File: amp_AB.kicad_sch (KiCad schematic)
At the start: 15 parts, among them J1 Power, J2 Audio, J3 Conn_01x02, Q1 TIP141, Q2 TIP146, U2 NE5532

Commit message: EL HUEVO SAPE
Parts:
- added C5, C6: 100n, Capacitor_SMD:CP_Elec_10x10, symbol ltspice:cap
- added C7, C8: 470µ, symbol ltspice:polcap
- C1: footprint (none) -> Capacitor_THT:CP_Radial_D13.0mm_P7.50mm
- C4: footprint (none) -> Capacitor_THT:CP_Radial_D10.0mm_P7.50mm
- R3: footprint (none) -> Resistor_SMD:R_01005_0402Metric
- R4: footprint (none) -> Resistor_THT:R_Axial_DIN0918_L18.0mm_D9.0mm_P25.40mm_Horizontal
- R5, R6: footprint (none) -> Resistor_THT:R_Axial_DIN0207_L6.3mm_D2.5mm_P10.16mm_Horizontal
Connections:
- net GND: now also C5.1, C6.1, C7.2 (B), C8.1 (A)
- net VCC: now also C6.2, C7.1 (A)
- net VEE: now also C5.2, C8.2 (B)

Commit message: agregue los footprints faltantes. Esquematico terminado
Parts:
- C1: footprint Capacitor_THT:CP_Radial_D13.0mm_P7.50mm -> Capacitor_THT:C_Rect_L11.5mm_W6.9mm_P10.00mm_MKT
- C2, C7, C8: footprint (none) -> Capacitor_THT:CP_Radial_D8.0mm_P3.50mm
- C3: footprint (none) -> Capacitor_THT:CP_Radial_D10.0mm_P5.00mm
- C4: footprint Capacitor_THT:CP_Radial_D10.0mm_P7.50mm -> Capacitor_THT:C_Disc_D5.0mm_W2.5mm_P5.00mm
- C5, C6: footprint Capacitor_SMD:CP_Elec_10x10 -> Capacitor_THT:C_Rect_L7.0mm_W3.5mm_P5.00mm
- J3: footprint TerminalBlock:TerminalBlock_MaiXu_MX126-5.0-02P_1x02_P5.00mm -> TerminalBlock:TerminalBlock_bornier-2_P5.08mm
- R3: footprint Resistor_SMD:R_01005_0402Metric -> Resistor_THT:R_Axial_DIN0207_L6.3mm_D2.5mm_P10.16mm_Horizontal
- R4: footprint Resistor_THT:R_Axial_DIN0918_L18.0mm_D9.0mm_P25.40mm_Horizontal -> Resistor_THT:R_Axial_DIN0207_L6.3mm_D2.5mm_P10.16mm_Horizontal
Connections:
- net at C2.2 (B): now also RV1.2; no longer RV1.1
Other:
- moved on the sheet: C3, RV1
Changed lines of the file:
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@@
 	)
 	(junction
-		(at 175.26 99.06)
+		(at 170.18 99.06)
 		(diameter 0)
 		(color 0 0 0 0)
 	)
 	(junction
-		(at 170.18 99.06)
+		(at 175.26 99.06)
 		(diameter 0)
 		(color 0 0 0 0)
@@
 	)
 	(junction
-		(at 139.7 147.32)
+		(at 135.89 147.32)
 		(diameter 0)
 		(color 0 0 0 0)
@@
 	(wire
 		(pts
-			(xy 139.7 147.32) (xy 139.7 148.59)
+			(xy 135.89 147.32) (xy 135.89 148.59)
 		)
 		(stroke
@@
 	(wire
 		(pts
-			(xy 181.61 99.06) (xy 200.66 99.06)
+			(xy 139.7 134.62) (xy 139.7 140.97)
 		)
 		(stroke
-			(width 0.1524)
-			(type solid)
+			(width 0)
+			(type default)
 		)
 	)
 	(wire
 		(pts
-			(xy 64.77 96.52) (xy 69.85 96.52)
+			(xy 185.42 99.06) (xy 200.66 99.06)
 		)
 		(stroke
-			(width 0)
-			(type default)
+			(width 0.1524)
+			(type solid)
 		)
 	)
 	(wire
 		(pts
-			(xy 139.7 137.16) (xy 139.7 134.62)
+			(xy 64.77 96.52) (xy 69.85 96.52)
 		)
 		(stroke
-			(width 0.1524)
-			(type solid)
+			(width 0)
+			(type default)
 		)
 	)
@@
 	(wire
 		(pts
-			(xy 176.53 99.06) (xy 175.26 99.06)
+			(xy 180.34 99.06) (xy 175.26 99.06)
 		)
 		(stroke
@@
 	(wire
 		(pts
-			(xy 139.7 144.78) (xy 139.7 147.32)
+			(xy 135.89 144.78) (xy 135.89 147.32)
 		)
 		(stroke
@@
 			)
 		)
-		(property "Footprint" ""
+		(property "Footprint" "Capacitor_THT:CP_Radial_D8.0mm_P3.50mm"
 			(at 138.43 129.54 0)
 			(hide yes)
@@
 	(symbol
 		(lib_id "Device:R_Potentiometer")
-		(at 139.7 140.97 0)
+		(at 135.89 140.97 0)
 		(unit 1)
 		(body_style 1)
@@
 		(fields_autoplaced yes)
 		(property "Reference" "RV1"
-			(at 137.16 139.6999 0)
+			(at 133.35 139.6999 0)
 			(show_name no)
 			(do_not_autoplace no)
@@
 		)
 		(property "Value" "10k_V"
-			(at 137.16 142.2399 0)
+			(at 133.35 142.2399 0)
 			(show_name no)
 			(do_not_autoplace no)
@@
 		)
 		(property "Footprint" "Potentiometer_THT:Potentiometer_Alps_RK163_Single_Horizontal"
-			(at 139.7 140.97 0)
+			(at 135.89 140.97 0)
 			(hide yes)
 			(show_name no)
@@
 		)
 		(property "Datasheet" ""
-			(at 139.7 140.97 0)
+			(at 135.89 140.97 0)
 			(hide yes)
 			(show_name no)
@@
 		)
 		(property "Description" "Potentiometer"
-			(at 139.7 140.97 0)
+			(at 135.89 140.97 0)
 			(hide yes)
 			(show_name no)
@@
 			)
 		)
-		(property "Footprint" "Resistor_SMD:R_01005_0402Metric"
+		(property "Footprint" "Resistor_THT:R_Axial_DIN0207_L6.3mm_D2.5mm_P10.16mm_Horizontal"
 			(at 162.56 127 0)
 			(hide yes)
@@
 	(symbol
 		(lib_id "power:GND")
-		(at 139.7 148.59 0)
+		(at 135.89 148.59 0)
 		(unit 1)
 		(body_style 1)
@@
 		(fields_autoplaced yes)
 		(property "Reference" "#PWR06"
-			(at 139.7 154.94 0)
+			(at 135.89 154.94 0)
 			(hide yes)
 			(show_name no)
@@
 		)
 		(property "Value" "GND"
-			(at 139.7 153.67 0)
+			(at 135.89 153.67 0)
 			(show_name no)
 			(do_not_autoplace no)
@@
 		)
 		(property "Footprint" ""
-			(at 139.7 148.59 0)
+			(at 135.89 148.59 0)
 			(hide yes)
 			(show_name no)
@@
 		)
 		(property "Datasheet" ""
-			(at 139.7 148.59 0)
+			(at 135.89 148.59 0)
 			(hide yes)
 			(show_name no)
@@
 		)
 		(property "Description" "Power symbol creates a global label with name \"GND\" , ground"
-			(at 139.7 148.59 0)
+			(at 135.89 148.59 0)
 			(hide yes)
 			(show_name no)
@@
 			)
 		)
-		(property "Footprint" ""
+		(property "Footprint" "Capacitor_THT:CP_Radial_D8.0mm_P3.50mm"
 			(at 71.12 83.82 0)
 			(hide yes)
@@
 	(symbol
 		(lib_id "ltspice:polcap")
-		(at 176.53 97.79 90)
+		(at 180.34 97.79 90)
 		(mirror x)
 		(unit 1)
@@
 		(dnp no)
 		(property "Reference" "C3"
-			(at 179.07 97.79 90)
+			(at 182.88 97.79 90)
 			(show_name no)
 			(do_not_autoplace no)
@@
 		)
 		(property "Value" "1m"
-			(at 179.07 100.33 90)
+			(at 182.88 100.33 90)
 			(show_name no)
 			(do_not_autoplace no)
@@
 			)
 		)
-		(property "Footprint" ""
-			(at 176.53 97.79 0)
+		(property "Footprint" "Capacitor_THT:CP_Radial_D10.0mm_P5.00mm"
+			(at 180.34 97.79 0)
 			(hide yes)
 			(show_name no)
@@
 		)
 		(property "Datasheet" ""
-			(at 176.53 97.79 0)
+			(at 180.34 97.79 0)
 			(hide yes)
 			(show_name no)
@@
 		)
 		(property "Description" ""
-			(at 176.53 97.79 0)
+			(at 180.34 97.79 0)
 			(hide yes)
 			(show_name no)
@@
 		)
 		(property "Sim.Device" "C"
-			(at 176.53 97.79 0)
+			(at 180.34 97.79 0)
 			(hide yes)
 			(show_name no)
@@
 		)
 		(property "Sim.Params" "C=${VALUE}"
-			(at 176.53 97.79 0)
+			(at 180.34 97.79 0)
 			(hide yes)
 			(show_name no)
@@
 	(symbol
 		(lib_id "power:PWR_FLAG")
-		(at 139.7 147.32 90)
+		(at 135.89 147.32 90)
 		(unit 1)
 		(body_style 1)
@@
 		(fields_autoplaced yes)
 		(property "Reference" "#FLG01"
-			(at 137.795 147.32 0)
+			(at 133.985 147.32 0)
 			(hide yes)
 			(show_name no)
@@
 		)
 		(property "Value" "GND"
-			(at 135.89 147.3199 90)
+			(at 132.08 147.3199 90)
 			(show_name no)
 			(do_not_autoplace no)
@@
 		)
 		(property "Footprint" ""
-			(at 139.7 147.32 0)
+			(at 135.89 147.32 0)
 			(hide yes)
 			(show_name no)
@@
 		)
 		(property "Datasheet" ""
-			(at 139.7 147.32 0)
+			(at 135.89 147.32 0)
 			(hide yes)
 			(show_name no)
@@
 		)
 		(property "Description" "Special symbol for telling ERC where power comes from"
-			(at 139.7 147.32 0)
+			(at 135.89 147.32 0)
 			(hide yes)
 			(show_name no)
@@
 			)
 		)
-		(property "Footprint" "TerminalBlock:TerminalBlock_MaiXu_MX126-5.0-02P_1x02_P5.00mm"
+		(property "Footprint" "TerminalBlock:TerminalBlock_bornier-2_P5.08mm"
 			(at 205.74 99.06 0)
 			(hide yes)
@@
 			)
 		)
-		(property "Footprint" ""
+		(property "Footprint" "Capacitor_THT:CP_Radial_D8.0mm_P3.50mm"
 			(at 73.66 73.66 0)
 			(hide yes)
@@
 			)
 		)
-		(property "Footprint" "Capacitor_THT:CP_Radial_D10.0mm_P7.50mm"
+		(property "Footprint" "Capacitor_THT:C_Disc_D5.0mm_W2.5mm_P5.00mm"
 			(at 158.75 85.09 0)
 			(hide yes)
@@
 			)
 		)
-		(property "Footprint" "Capacitor_THT:CP_Radial_D13.0mm_P7.50mm"
+		(property "Footprint" "Capacitor_THT:C_Rect_L11.5mm_W6.9mm_P10.00mm_MKT"
 			(at 127 93.98 0)
 			(hide yes)
@@
 			)
 		)
-		(property "Footprint" "Capacitor_SMD:CP_Elec_10x10"
+		(property "Footprint" "Capacitor_THT:C_Rect_L7.0mm_W3.5mm_P5.00mm"
 			(at 152.4 111.76 0)
 			(hide yes)
@@
 			)
 		)
-		(property "Footprint" "Resistor_THT:R_Axial_DIN0918_L18.0mm_D9.0mm_P25.40mm_Horizontal"
+		(property "Footprint" "Resistor_THT:R_Axial_DIN0207_L6.3mm_D2.5mm_P10.16mm_Horizontal"
 			(at 129.54 93.98 0)
 			(hide yes)
@@
 			)
 		)
-		(property "Footprint" "Capacitor_SMD:CP_Elec_10x10"
+		(property "Footprint" "Capacitor_THT:C_Rect_L7.0mm_W3.5mm_P5.00mm"
 			(at 139.7 88.9 0)
 			(hide yes)

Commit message: primer diseño de pcb
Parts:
- removed RV1: 10k_V, Potentiometer_THT:Potentiometer_Alps_RK163_Single_Horizontal, symbol Device:R_Potentiometer
- added J4: Pot_10k, Connector_Molex:Molex_KK-254_AE-6410-03A_1x03_P2.54mm_Vertical, symbol Connector_Generic:Conn_01x03
- C1: footprint Capacitor_THT:C_Rect_L11.5mm_W6.9mm_P10.00mm_MKT -> Capacitor_THT:C_Rect_L13.0mm_W6.0mm_P10.00mm_FKS3_FKP3_MKS4
- C7, C8: value 470µ -> 22µ; footprint Capacitor_THT:CP_Radial_D8.0mm_P3.50mm -> Capacitor_THT:CP_Radial_D10.0mm_P5.00mm
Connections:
- net GND: now also J4.3 (Pin_3)
- net at C2.2 (B): now also J4.2 (Pin_2)
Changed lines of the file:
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@@
 	(wire
 		(pts
-			(xy 139.7 134.62) (xy 139.7 140.97)
+			(xy 135.89 142.24) (xy 139.7 142.24)
+		)
+		(stroke
+			(width 0)
+			(type default)
+		)
+	)
+	(wire
+		(pts
+			(xy 139.7 134.62) (xy 139.7 142.24)
 		)
 		(stroke
@@
 	)
 	(symbol
-		(lib_id "Device:R_Potentiometer")
-		(at 135.89 140.97 0)
-		(unit 1)
-		(body_style 1)
-		(exclude_from_sim no)
-		(in_bom yes)
-		(on_board yes)
-		(in_pos_files yes)
-		(dnp no)
-		(fields_autoplaced yes)
-		(property "Reference" "RV1"
-			(at 133.35 139.6999 0)
-			(show_name no)
-			(do_not_autoplace no)
-			(effects
-				(font
-					(size 1.27 1.27)
-				)
-				(justify right)
-			)
-		)
-		(property "Value" "10k_V"
-			(at 133.35 142.2399 0)
-			(show_name no)
-			(do_not_autoplace no)
-			(effects
-				(font
-					(size 1.27 1.27)
-				)
-				(justify right)
-			)
-		)
-		(property "Footprint" "Potentiometer_THT:Potentiometer_Alps_RK163_Single_Horizontal"
-			(at 135.89 140.97 0)
-			(hide yes)
-			(show_name no)
-			(do_not_autoplace no)
-			(effects
-				(font
-					(size 1.27 1.27)
-				)
-			)
-		)
-		(property "Datasheet" ""
-			(at 135.89 140.97 0)
-			(hide yes)
-			(show_name no)
-			(do_not_autoplace no)
-			(effects
-				(font
-					(size 1.27 1.27)
-				)
-			)
-		)
-		(property "Description" "Potentiometer"
-			(at 135.89 140.97 0)
-			(hide yes)
-			(show_name no)
-			(do_not_autoplace no)
-			(effects
-				(font
-					(size 1.27 1.27)
-				)
-			)
-		)
-		(pin "2"
-		)
-		(pin "3"
-		)
-		(pin "1"
-		)
-		(instances
-			(project "amp_AB"
-				(path "/4a35f5ed-8223-47c1-ac47-274db02c443d"
-					(reference "RV1")
-					(unit 1)
-				)
-			)
-		)
-	)
-	(symbol
 		(lib_id "Amplifier_Operational:NE5532")
 		(at 147.32 97.79 0)
@@
 			)
 		)
-		(property "Value" "470µ"
+		(property "Value" "22µ"
 			(at 69.215 79.375 0)
 			(show_name no)
@@
 			)
 		)
-		(property "Footprint" "Capacitor_THT:CP_Radial_D8.0mm_P3.50mm"
+		(property "Footprint" "Capacitor_THT:CP_Radial_D10.0mm_P5.00mm"
 			(at 71.12 83.82 0)
 			(hide yes)
@@
 	)
 	(symbol
+		(lib_id "Connector_Generic:Conn_01x03")
+		(at 130.81 142.24 0)
+		(mirror y)
+		(unit 1)
+		(body_style 1)
+		(exclude_from_sim no)
+		(in_bom yes)
+		(on_board yes)
+		(in_pos_files yes)
+		(dnp no)
+		(property "Reference" "J4"
+			(at 128.27 140.9699 0)
+			(show_name no)
+			(do_not_autoplace no)
+			(effects
+				(font
+					(size 1.27 1.27)
+				)
+				(justify left)
+			)
+		)
+		(property "Value" "Pot_10k"
+			(at 128.27 143.5099 0)
+			(show_name no)
+			(do_not_autoplace no)
+			(effects
+				(font
+					(size 1.27 1.27)
+				)
+				(justify left)
+			)
+		)
+		(property "Footprint" "Connector_Molex:Molex_KK-254_AE-6410-03A_1x03_P2.54mm_Vertical"
+			(at 130.81 142.24 0)
+			(hide yes)
+			(show_name no)
+			(do_not_autoplace no)
+			(effects
+				(font
+					(size 1.27 1.27)
+				)
+			)
+		)
+		(property "Datasheet" ""
+			(at 130.81 142.24 0)
+			(hide yes)
+			(show_name no)
+			(do_not_autoplace no)
+			(effects
+				(font
+					(size 1.27 1.27)
+				)
+			)
+		)
+		(property "Description" "Generic connector, single row, 01x03, script generated (kicad-library-utils/schlib/autogen/connector/)"
+			(at 130.81 142.24 0)
+			(hide yes)
+			(show_name no)
+			(do_not_autoplace no)
+			(effects
+				(font
+					(size 1.27 1.27)
+				)
+			)
+		)
+		(pin "1"
+		)
+		(pin "2"
+		)
+		(pin "3"
+		)
+		(instances
+			(project "amp_AB"
+				(path "/4a35f5ed-8223-47c1-ac47-274db02c443d"
+					(reference "J4")
+					(unit 1)
+				)
+			)
+		)
+	)
+	(symbol
 		(lib_id "ltspice:polcap")
 		(at 180.34 97.79 90)
@@
 			)
 		)
-		(property "Value" "470µ"
+		(property "Value" "22µ"
 			(at 75.565 78.105 0)
 			(show_name no)
@@
 			)
 		)
-		(property "Footprint" "Capacitor_THT:CP_Radial_D8.0mm_P3.50mm"
+		(property "Footprint" "Capacitor_THT:CP_Radial_D10.0mm_P5.00mm"
 			(at 73.66 73.66 0)
 			(hide yes)
@@
 			)
 		)
-		(property "Footprint" "Capacitor_THT:C_Rect_L11.5mm_W6.9mm_P10.00mm_MKT"
+		(property "Footprint" "Capacitor_THT:C_Rect_L13.0mm_W6.0mm_P10.00mm_FKS3_FKP3_MKS4"
 			(at 127 93.98 0)
 			(hide yes)

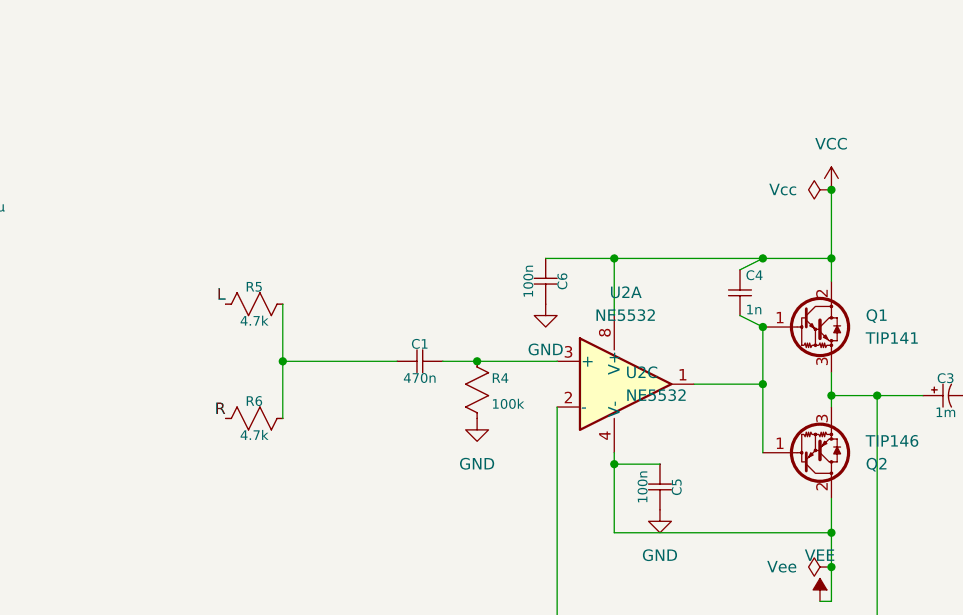
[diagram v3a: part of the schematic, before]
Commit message: Termine el routing y puse los mounting holes
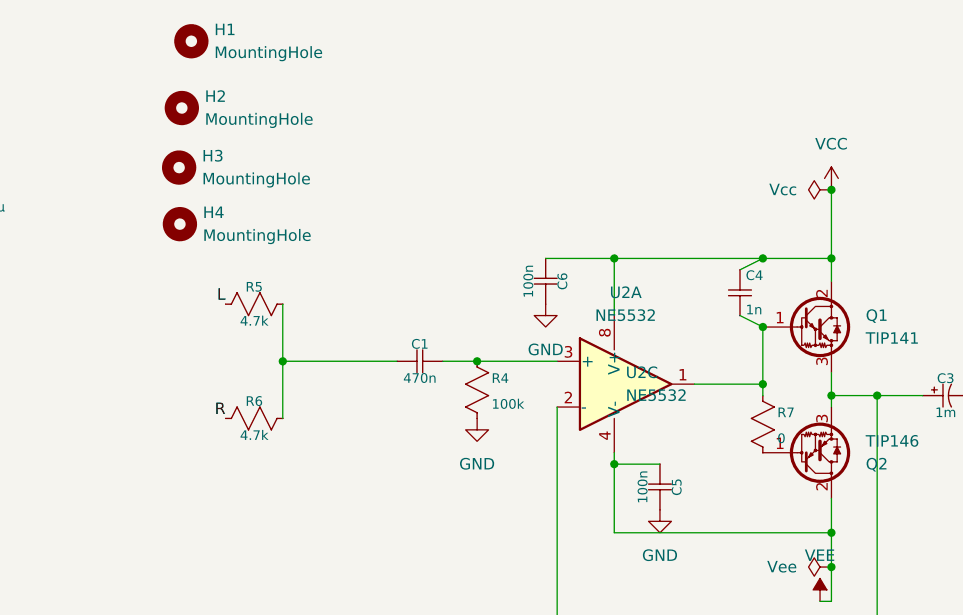
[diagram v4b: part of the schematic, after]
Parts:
- added H1, H2, H3, H4: MountingHole, MountingHole:MountingHole_3.2mm_M3, symbol Mechanical:MountingHole
- added R7: 0, Resistor_THT:R_Axial_DIN0207_L6.3mm_D2.5mm_P10.16mm_Horizontal, symbol ltspice:res
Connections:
- net at C4.2, Q1.1 (B), U2.1: now also R7.1; no longer Q2.1 (B)
- new net: Q2.1 (B), R7.2

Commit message: Corregidas las islas desconectadas
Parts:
- C6: footprint Capacitor_THT:C_Rect_L7.0mm_W3.5mm_P5.00mm -> Capacitor_THT:C_Rect_L10.0mm_W4.0mm_P7.50mm_MKS4
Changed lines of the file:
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@@
 			)
 		)
-		(property "Footprint" "Capacitor_THT:C_Rect_L7.0mm_W3.5mm_P5.00mm"
+		(property "Footprint" "Capacitor_THT:C_Rect_L10.0mm_W4.0mm_P7.50mm_MKS4"
 			(at 139.7 88.9 0)
 			(hide yes)
